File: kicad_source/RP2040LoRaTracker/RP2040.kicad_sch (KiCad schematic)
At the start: 34 parts, among them J1 USB_B_Micro, J2 BM04B-SRSS-TB, SW1 SW_Push, SW2 SW_Push, U1 RP2040, U4 W25Q16JVSS, Y1 Crystal_GND24_Small

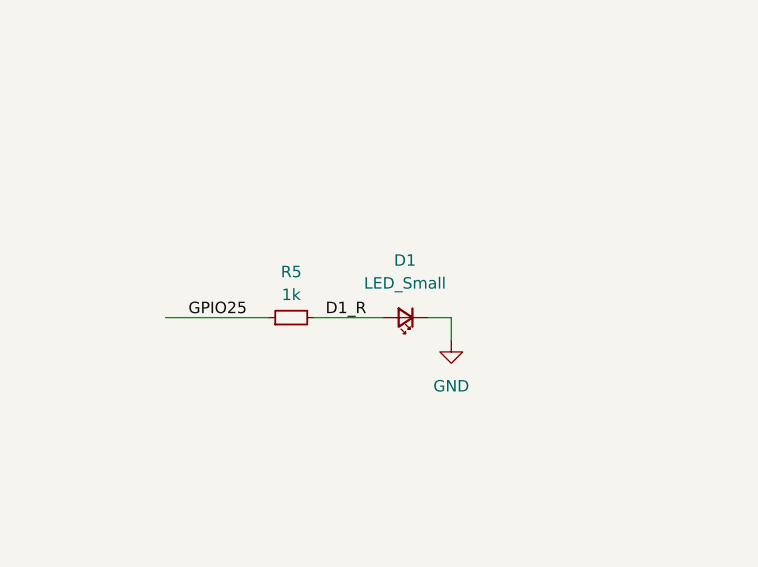
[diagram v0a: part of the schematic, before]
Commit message: added battery voltage measurement, R17 and R18
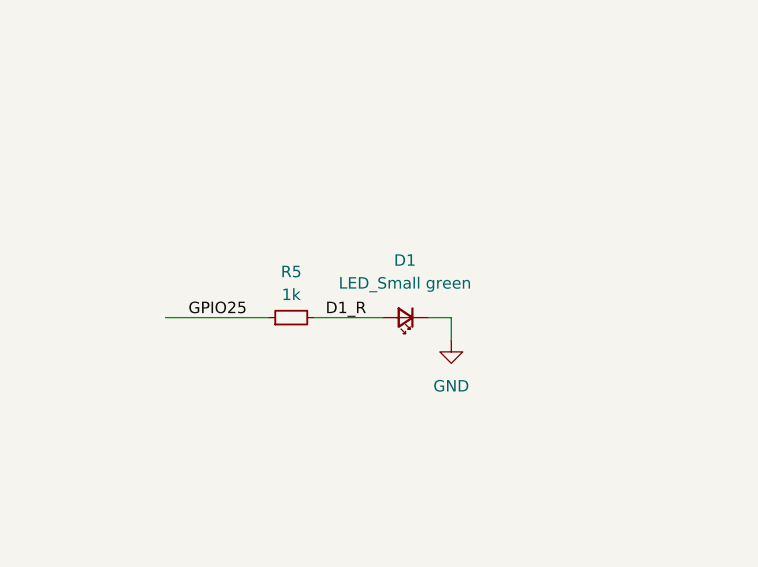
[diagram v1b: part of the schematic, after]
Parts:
- D1: value LED_Small -> LED_Small green
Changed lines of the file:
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@@
 			)
 		)
-		(property "Value" "LED_Small"
+		(property "Value" "LED_Small green"
 			(at 239.9665 133.35 0)
 			(effects

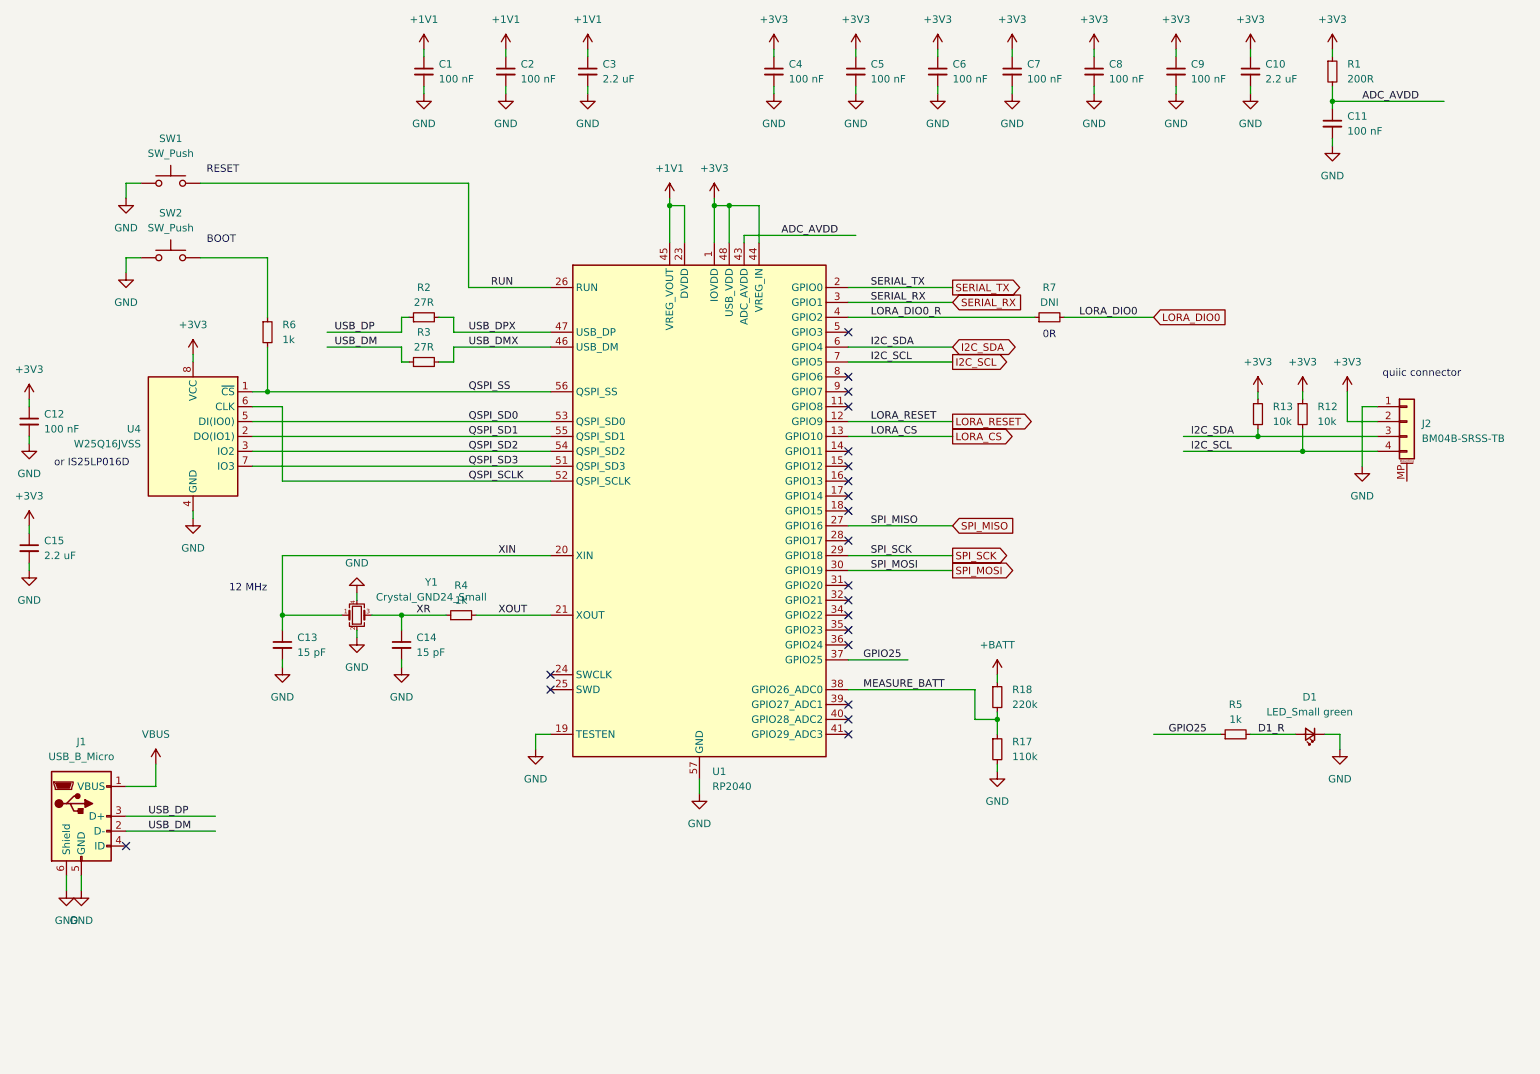
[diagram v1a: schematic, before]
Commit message: added compatibility for LoRa module Ra-01S, added R20 and R21
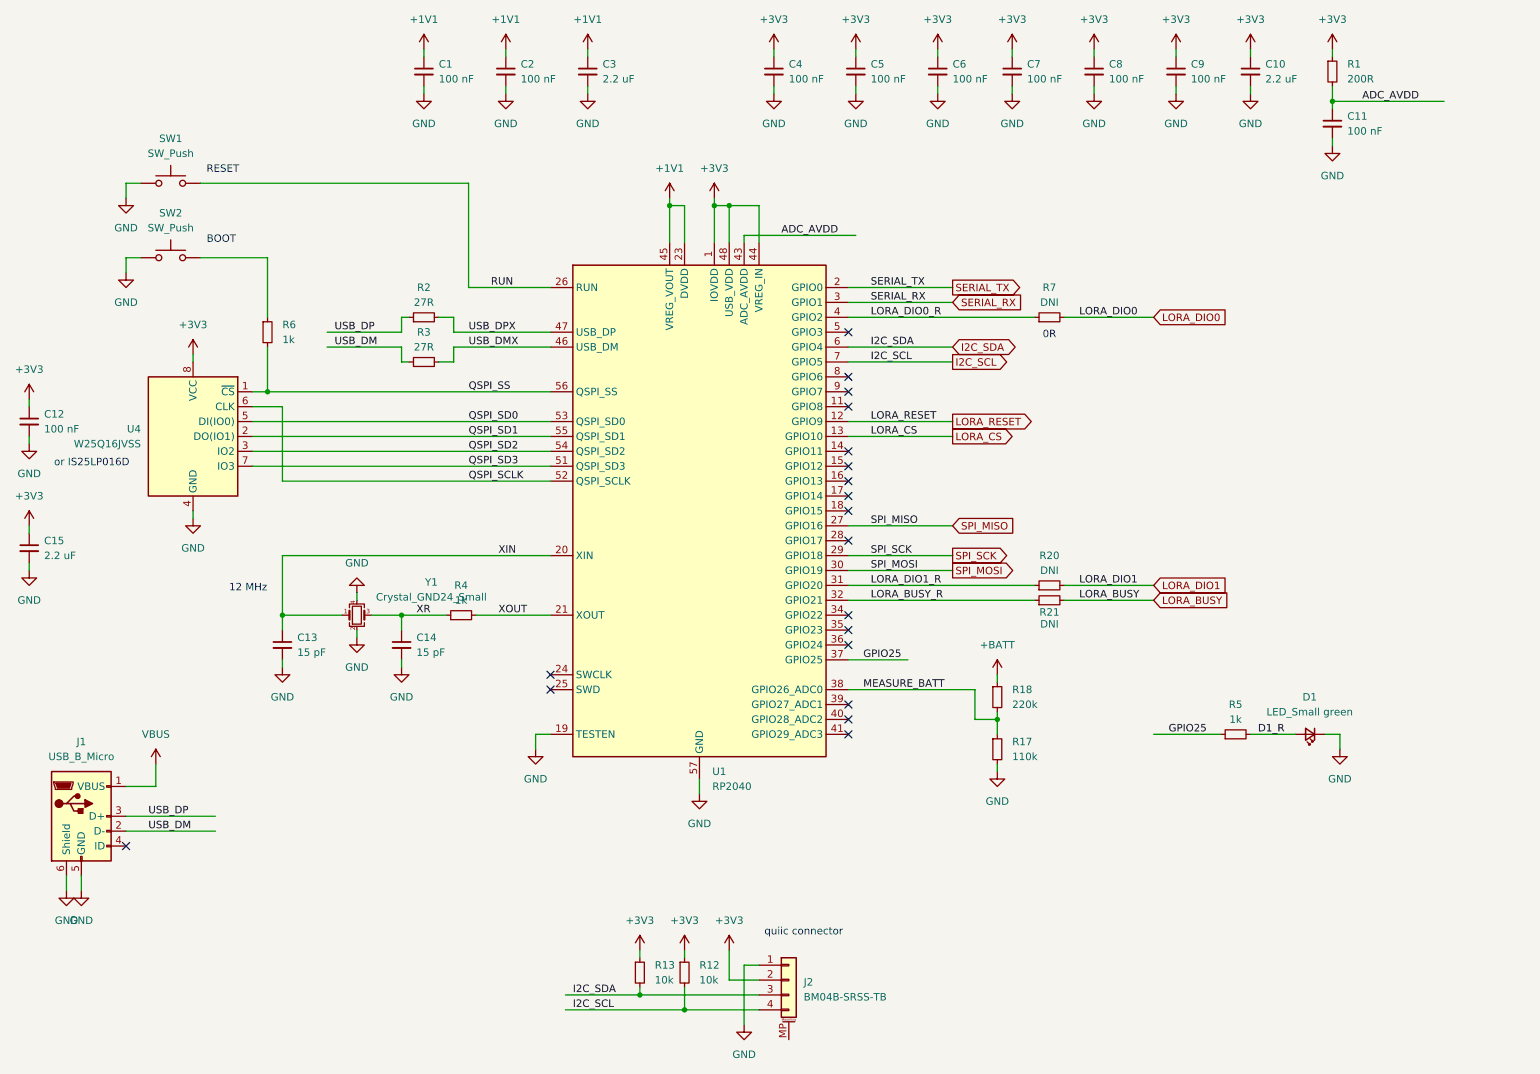
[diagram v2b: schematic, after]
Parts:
- added R20, R21: DNI, Resistor_SMD:R_0603_1608Metric, symbol Device:R_Small
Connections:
- net LORA_DIO1_R: now reaches U1.31 (GPIO20)
- net LORA_DIO1_R: now also R20.1
- net LORA_BUSY_R: now reaches U1.32 (GPIO21)
- net LORA_BUSY_R: now also R21.1
- new net LORA_BUSY: R21.2
- new net LORA_DIO1: R20.2
- no-connect marks 21 -> 19
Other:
- moved on the sheet: J2, R12, R13
